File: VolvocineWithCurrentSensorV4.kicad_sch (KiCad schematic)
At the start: 30 parts, among them J2 Conn_01x12_Socket, J3 Sensors, J4 Switch, J5 battery, J6 Conn_01x12_Socket, Q2 Si2319CDS, U1 PAM2401SCADJ, U2 PIC10F322-IOT, U3 INA226

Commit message: SCH Save: 2 files changed VolvocineWithCurrentSensorV4.kicad_pro 12/0/2 VolvocineWithCurrentSensorV4.kicad_sch 1058/0/519
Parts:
- ServoMotor1: value ~ -> (none)

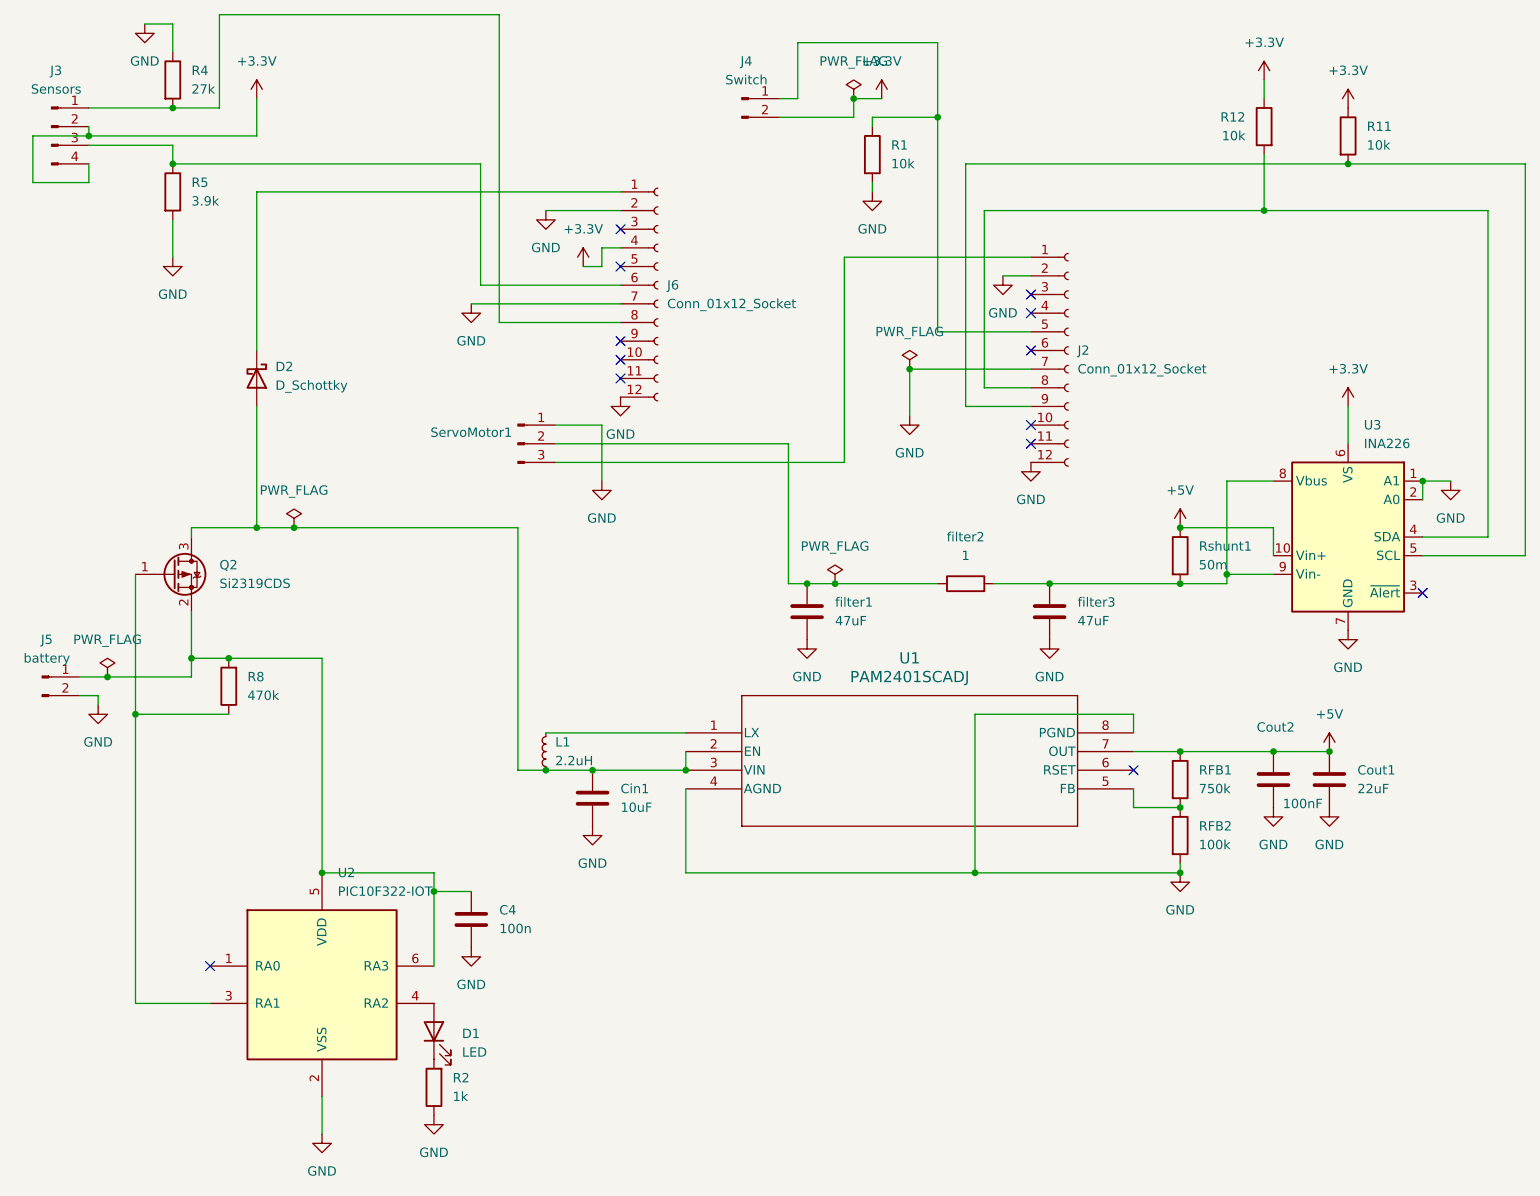
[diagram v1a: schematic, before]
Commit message: Update component values in schematic and add backup files
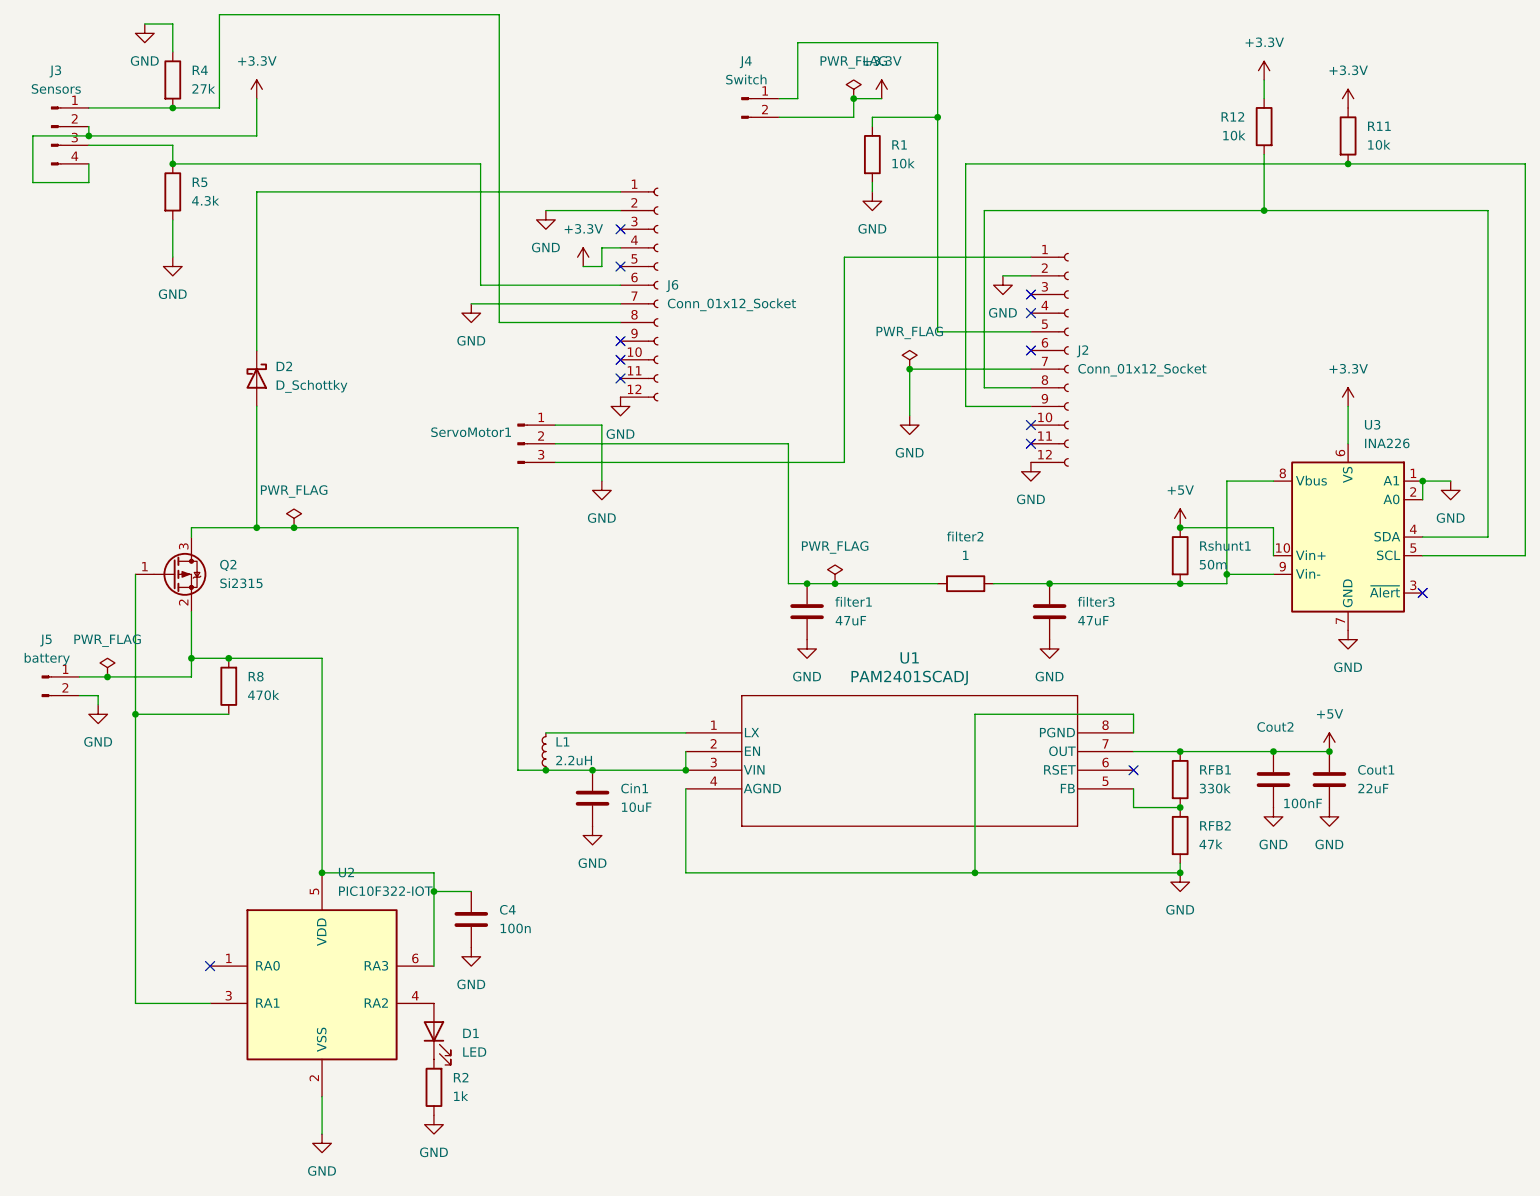
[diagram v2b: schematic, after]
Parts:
- Q2: value Si2319CDS -> Si2315
- R5: value 3.9k -> 4.3k
- RFB1: value 750k -> 330k
- RFB2: value 100k -> 47k
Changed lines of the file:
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@@
 			)
 		)
-		(property "Value" "Si2319CDS"
+		(property "Value" "Si2315"
 			(at 50.8 109.2199 0)
 			(show_name no)
@@
 			)
 		)
-		(property "Value" "3.9k"
+		(property "Value" "4.3k"
 			(at 46.99 57.1499 0)
 			(show_name no)
@@
 			)
 		)
-		(property "Value" "100k"
+		(property "Value" "47k"
 			(at 184.15 144.7799 0)
 			(show_name no)
@@
 			)
 		)
-		(property "Value" "750k"
+		(property "Value" "330k"
 			(at 184.15 137.1599 0)
 			(show_name no)
